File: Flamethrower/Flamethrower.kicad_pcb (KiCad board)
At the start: 2 copper layers, 76.2 x 99.1 mm, 57 parts, among them J201 USB_B_Micro, J301 JST_2MM_MALE, J302 BATT_EN, J303 5V_EN, J305 ADC_0, J306 ADC_1, J307 EXPANSION_0, J308 EXPANSION_1, J309 I2C_DEBUG, J310 SPARK, J311 PROG, J312 SERVO_0, J313 SERVO_1, Q301 TIP120, SW201 RST, SW202 Rotary_Encoder_Switch_1, SW203 Rotary_Encoder_Switch_0, U201 ADXL345-SF, U203 Pico, U204 LM2937xS, U301 MCP73831, U302 PAM2401

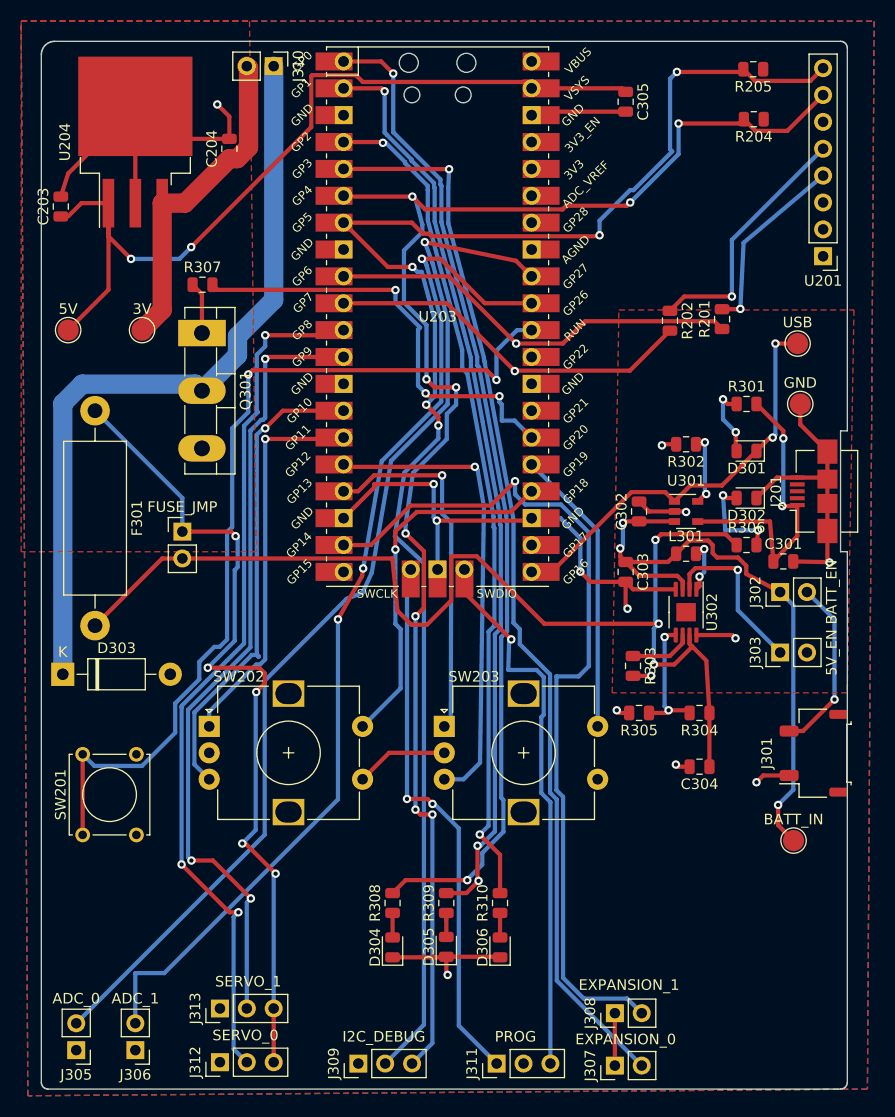
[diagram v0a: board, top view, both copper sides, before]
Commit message: Redit the PCB entirely
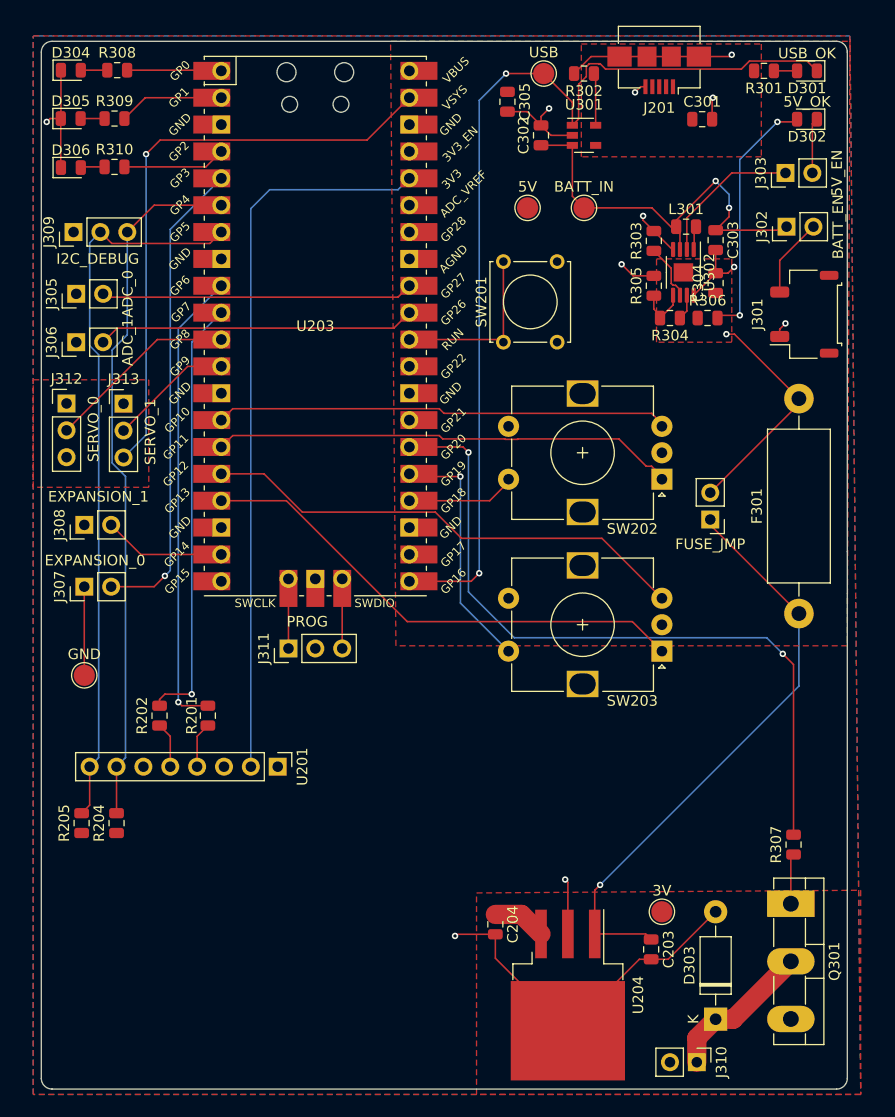
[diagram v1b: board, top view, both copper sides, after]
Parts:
- moved J310 102.3 mm to (112.8, 161.3)
- moved R205 95.5 mm to (54.6, 138.7), turned to 90 degrees
- moved U204 90.4 mm to (100.6, 154.9), turned to 270 degrees
- moved R204 89.8 mm to (57.9, 138.7), turned to 90 degrees
- moved C203 89.7 mm to (108.5, 150.6), turned to 270 degrees
- moved D304 88.3 mm to (53.6, 67.5), turned to 0 degrees
- moved D305 86.0 mm to (53.6, 72.1), turned to 0 degrees
- moved D306 84.2 mm to (53.6, 76.7), turned to 0 degrees
- moved J309 83.1 mm to (53.8, 82.8)
- moved R308 82.9 mm to (58.0, 67.5), turned to 0 degrees
- moved R309 80.5 mm to (57.7, 72.1), turned to 0 degrees
- moved R310 78.6 mm to (57.7, 76.6), turned to 0 degrees
- moved Q301 77.5 mm to (121.7, 146.3)
- moved C204 77.5 mm to (93.7, 148.3), turned to 270 degrees
- moved R307 77.0 mm to (121.9, 140.7), turned to 90 degrees
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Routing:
- net LED_0: track 94.1 -> 8.93 mm, vias 2 -> 0
- net /Sheet600348E6/BOOST_OUT: track 106.5 -> 24.1 mm, vias 3 -> 1
- net I2C_SCL: track 147.8 -> 68.7 mm, vias 5 -> 0
- net I2C_SDA: track 144.0 -> 66.4 mm, vias 9 -> 0
- net LED_1: track 86.1 -> 9.97 mm, vias 3 -> 0
- net EXP_1: track 82.1 -> 11.6 mm, vias 1 -> 0
- net ADC_0: track 99.2 -> 29.5 mm, vias 1 -> 0
- net /MCU/RST: track 86.2 -> 16.6 mm, vias 2 -> 0
- net LED_2: track 79.0 -> 9.76 mm, vias 2 -> 0
- net +3V3: track 0.00 -> 68.9 mm
- net ADC_1: track 97.3 -> 30.1 mm, vias 3 -> 0
- net SERVO_0: track 83.1 -> 18.2 mm, vias 3 -> 0
- net SERVO_1: track 75.8 -> 11.8 mm, vias 3 -> 0
- net /MCU/Pinouts/SPRK_FET: track 73.3 -> 14.2 mm
- net EXP_0: track 100.5 -> 45.3 mm
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- added copper zone on F.Cu, net /Sheet600348E6/BOOST_OUT
- added copper zone on F.Cu, net /Sheet600348E6/V_USB
- added copper zone on F.Cu, net 3V_SPRK
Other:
- outline, holes or cut-outs redrawn
- net class Default: clearance 0.2 -> 0.1524; trace_width 0.400558 -> 0.1524; via_dia 0.8 -> 0.6096; via_drill 0.4 -> 0.3048
- rule trace_clearance: 0.2 -> 0.1524
- rule trace_min: 0.2 -> 0.127
- rule via_min_drill: 0.3 -> 0.299999
- rule via_min_size: 0.4 -> 0.599999
